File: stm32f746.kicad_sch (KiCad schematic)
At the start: 30 parts, among them SW1 SW_SPDT, U1 STM32F746NGHx, X1 SG-5032CAN

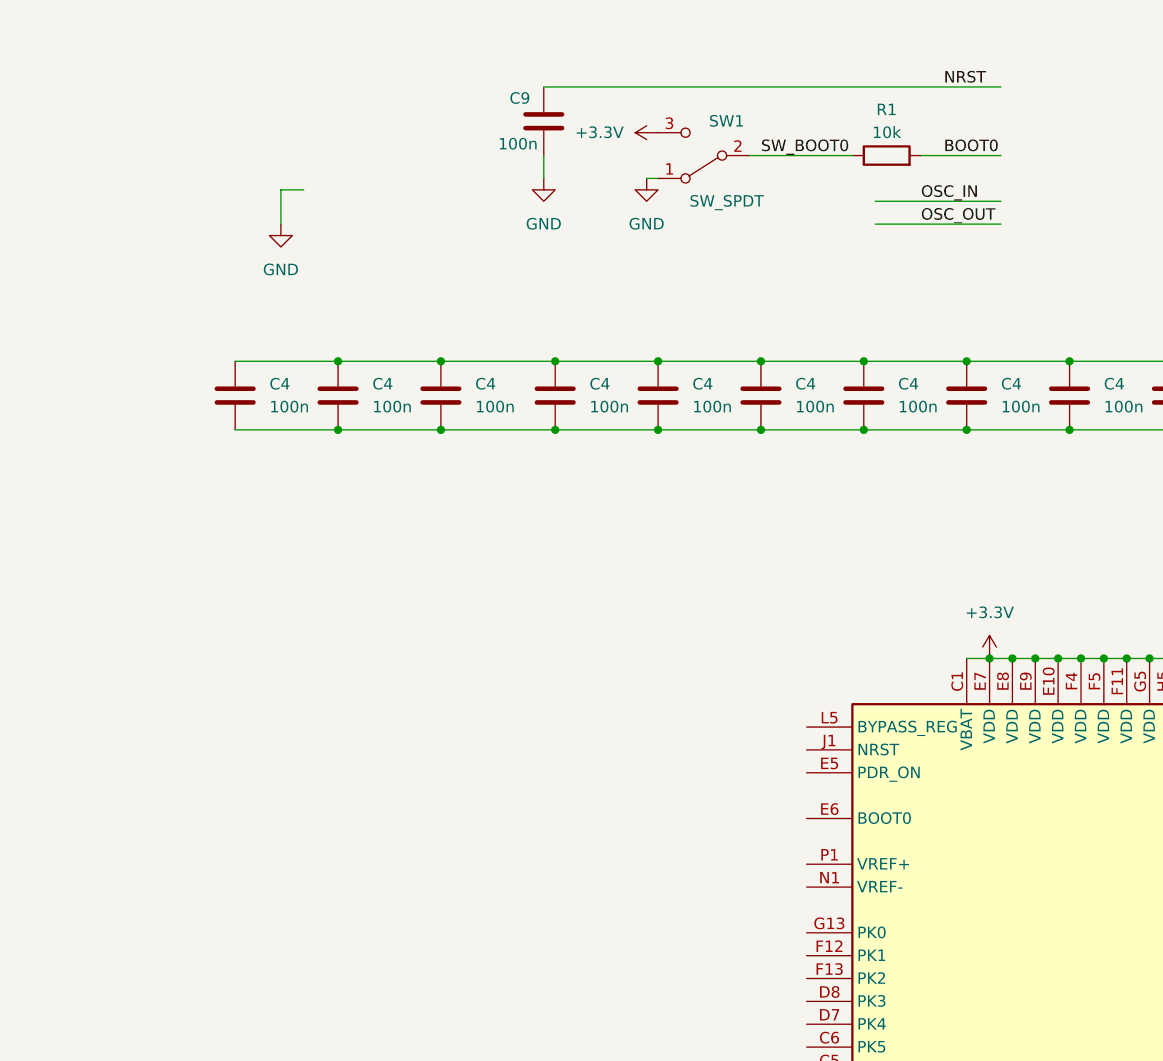
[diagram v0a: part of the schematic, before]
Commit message: add POE schematics, Ethernet phy
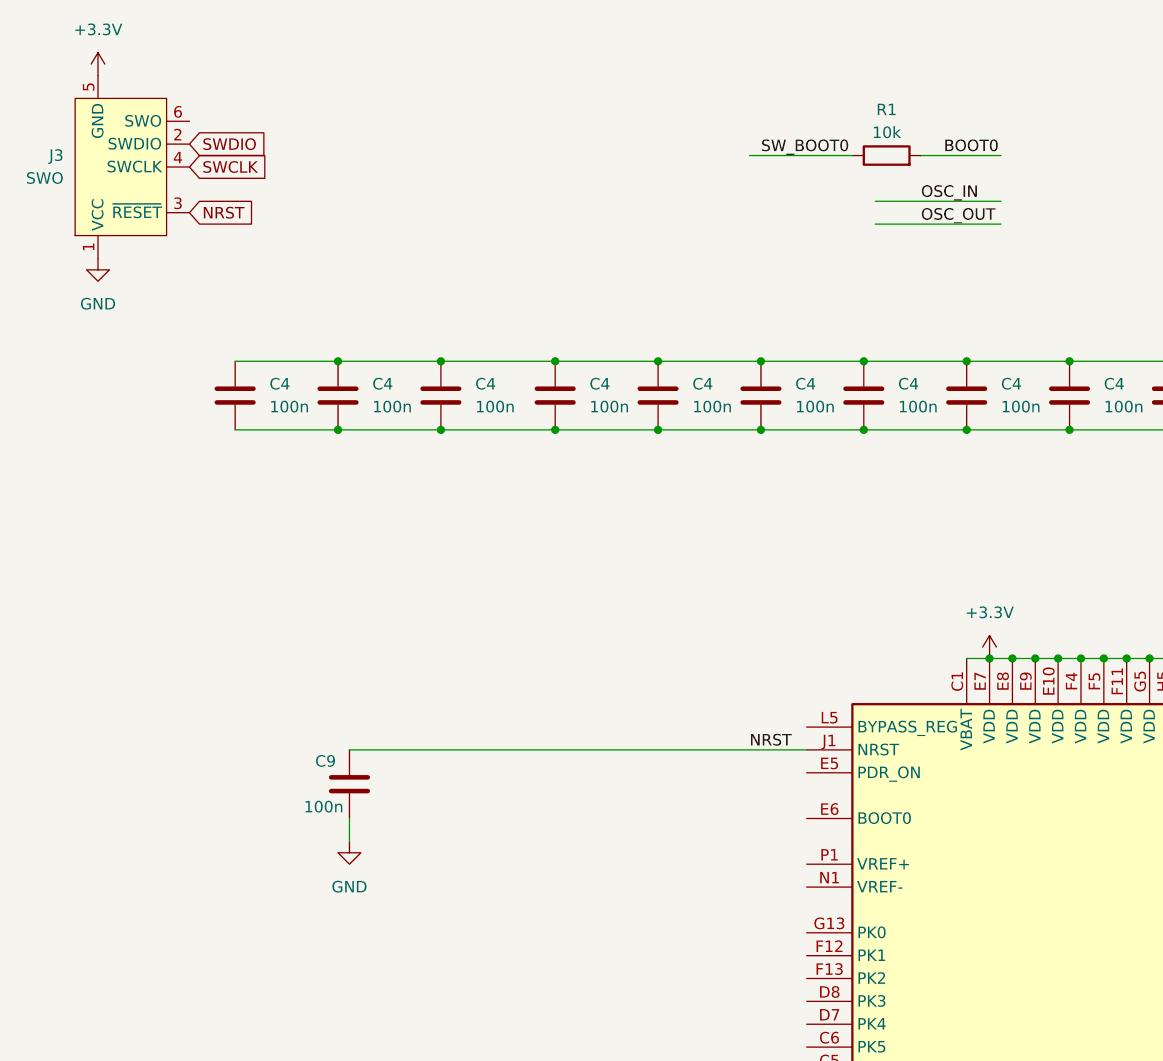
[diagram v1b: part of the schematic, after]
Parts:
- removed SW1: SW_SPDT, symbol Switch:SW_SPDT
- added J3: SWO, Connector:Tag-Connect_TC2030-IDC-NL_2x03_P1.27mm_Vertical, symbol Connector:Conn_ARM_SWD_TagConnect_TC2030-NL
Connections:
- net +3.3V: now also J3.5 (GND)
- net GND: now also J3.1 (VCC)
- net NRST: now also U1.J1 (NRST), J3.3 (~{RESET})
- net SWCLK: now also J3.4 (SWCLK)
- net SWDIO: now also J3.2 (SWDIO)
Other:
- moved on the sheet: C9

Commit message: almost final schematics
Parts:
- removed C9: 100n, Capacitor_SMD:C_0805_2012Metric, symbol Device:C
- removed R1: 10k, symbol Device:R
- added C4 (x2): 2.2uF, Capacitor_SMD:C_0603_1608Metric, symbol Device:C
- added C4: 100n, Capacitor_SMD:C_0402_1005Metric, symbol Device:C
- added R1 (x5): 10K, Resistor_SMD:R_0402_1005Metric, symbol Device:R
- added R1: 100, Resistor_SMD:R_0402_1005Metric, symbol Device:R
- added R1: 0, Resistor_SMD:R_0402_1005Metric, symbol Device:R
- added U13: W25Q128JVS, Package_SO:SOIC-8_5.23x5.23mm_P1.27mm, symbol Memory_Flash:W25Q128JVS
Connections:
- net +3.3V: now also U1.G11 (VDDUSB), X1.4 (VCC), C4.1, R1.2, R1.2, R1.2
- net +3.3VA: now also U1.R1 (VDDA), R1.2
- net GND: now also U1.F10 (VSS), U1.F2 (VSS), U1.F6 (VSS), U1.F7 (VSS), U1.F8 (VSS), U1.F9 (VSS), U1.G10 (VSS), U1.G6 (VSS), U1.H10 (VSS), U1.H6 (VSS), U1.J10 (VSS), U1.J6 (VSS), U1.K10 (VSS), U1.K6 (VSS), U1.K7 (VSS), U1.K8 (VSS), U1.K9 (VSS), U1.L6 (VSS), U1.M1 (VSSA), U1.N1 (VREF-), X1.2 (GND), C4.2, C4.2, C4.2, R1.2, R1.2
- net NRST: now also R1.1
- net OSC_IN: now also U1.G1 (PH0), R1.2
- net at X1.1 (~{ST}): now also R1.1
- net OSC_25M: now reaches X1.3 (OUT)
- net OSC_25M: now also R1.1
- net RMII_TXD1: now reaches U1.A4 (PG14)
- net FMC_NBL1: now reaches U1.A5 (PE1)
- net FMC_NBL0: now reaches U1.A6 (PE0)
- net CAN1_RX: now reaches U1.A7 (PB8)
- net CAN2_RX: now reaches U1.A8 (PB5)
- net FMC_D2: now reaches U1.B12 (PD0)
- net RMII_TXD0: now reaches U1.B3 (PG13)
- net CAN1_TX: now reaches U1.B4 (PB9)
- net CAN2_TX: now reaches U1.B6 (PB6)
- net FMC_SDNCAS: now reaches U1.B7 (PG15)
- net RMII_TX_EN: now reaches U1.B8 (PG11)
- net FMC_D3: now reaches U1.C12 (PD1)
- net FMC_A0: now reaches U1.D2 (PF0)
- net at U1.E11 (VCAP_2): now also C4.1
- net FMC_A1: now reaches U1.E2 (PF1)
- net at U1.E5 (PDR_ON): now also R1.1
- net at U1.E6 (BOOT0): now also R1.1
- net FMC_A2: now reaches U1.G2 (PF2)
- net FMC_SDCLK: now reaches U1.H14 (PG8)
- net FMC_A3: now reaches U1.H2 (PF3)
- net FMC_A4: now reaches U1.J2 (PF4)
- net FMC_SDNWE: now reaches U1.J3 (PH5)
- net FMC_SDNE0: now reaches U1.J4 (PH3)
- net FMC_D1: now reaches U1.K13 (PD15)
- net FMC_D15: now reaches U1.K15 (PD10)
- net FMC_A5: now reaches U1.K3 (PF5)
- net FMC_SDCKE0: now reaches U1.K4 (PH2)
- net at U1.L11 (VCAP_1): now also C4.1
- net FMC_D0: now reaches U1.L12 (PD14)
- net FMC_D14: now reaches U1.L14 (PD9)
- net FMC_D13: now reaches U1.L15 (PD8)
- net at U1.L5 (BYPASS_REG): now also R1.1
- net RMII_RXER: now reaches U1.M13 (PG2)
- net RMII_MDC: now reaches U1.M3 (PC1)
- net FMC_A6: now reaches U1.M6 (PF12)
- net FMC_A11: now reaches U1.M7 (PG1)
- net FMC_A8: now reaches U1.M8 (PF15)
- net FMC_A8: now also U1.P6 (PF14)
- net FMC_BA1: now reaches U1.N11 (PG5)
- net FMC_BA0: now reaches U1.N12 (PG4)
- net RMII_REF_CLK: now reaches U1.N2 (PA1)
- net RMII_RXD0: now reaches U1.N5 (PC4)
- net FMC_A7: now reaches U1.N6 (PF13)
- net FMC_A10: now reaches U1.N7 (PG0)
- net FMC_D5: now reaches U1.N9 (PE8)
- net at U1.P1 (VREF+): now also R1.1
- net FMC_D8: now reaches U1.P10 (PE11)
- net FMC_D11: now reaches U1.P11 (PE14)
- net RMII_MDIO: now reaches U1.P2 (PA2)
- net RMII_RXD1: now reaches U1.P5 (PC5)
- net FMC_SDNRAS: now reaches U1.P8 (PF11)
- net FMC_D6: now reaches U1.P9 (PE9)
- net FMC_D9: now reaches U1.R10 (PE12)
- net FMC_D12: now reaches U1.R11 (PE15)
- net FMC_D10: now reaches U1.R12 (PE13)
- net RMII_CRS_DV: now reaches U1.R3 (PA7)
- net FMC_D4: now reaches U1.R8 (PE7)
- net FMC_D7: now reaches U1.R9 (PE10)
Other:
- moved on the sheet: X1
